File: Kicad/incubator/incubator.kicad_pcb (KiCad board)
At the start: 2 copper layers, 36 parts, among them J1 Barrel_Jack_MountingPin, J3 Conn_02x03_Odd_Even, J4 RJ12, J5 Conn_01x05, SW2 Rotary_Encoder_Switch, U1 AP63205WU, U2 ATmega328P-AU

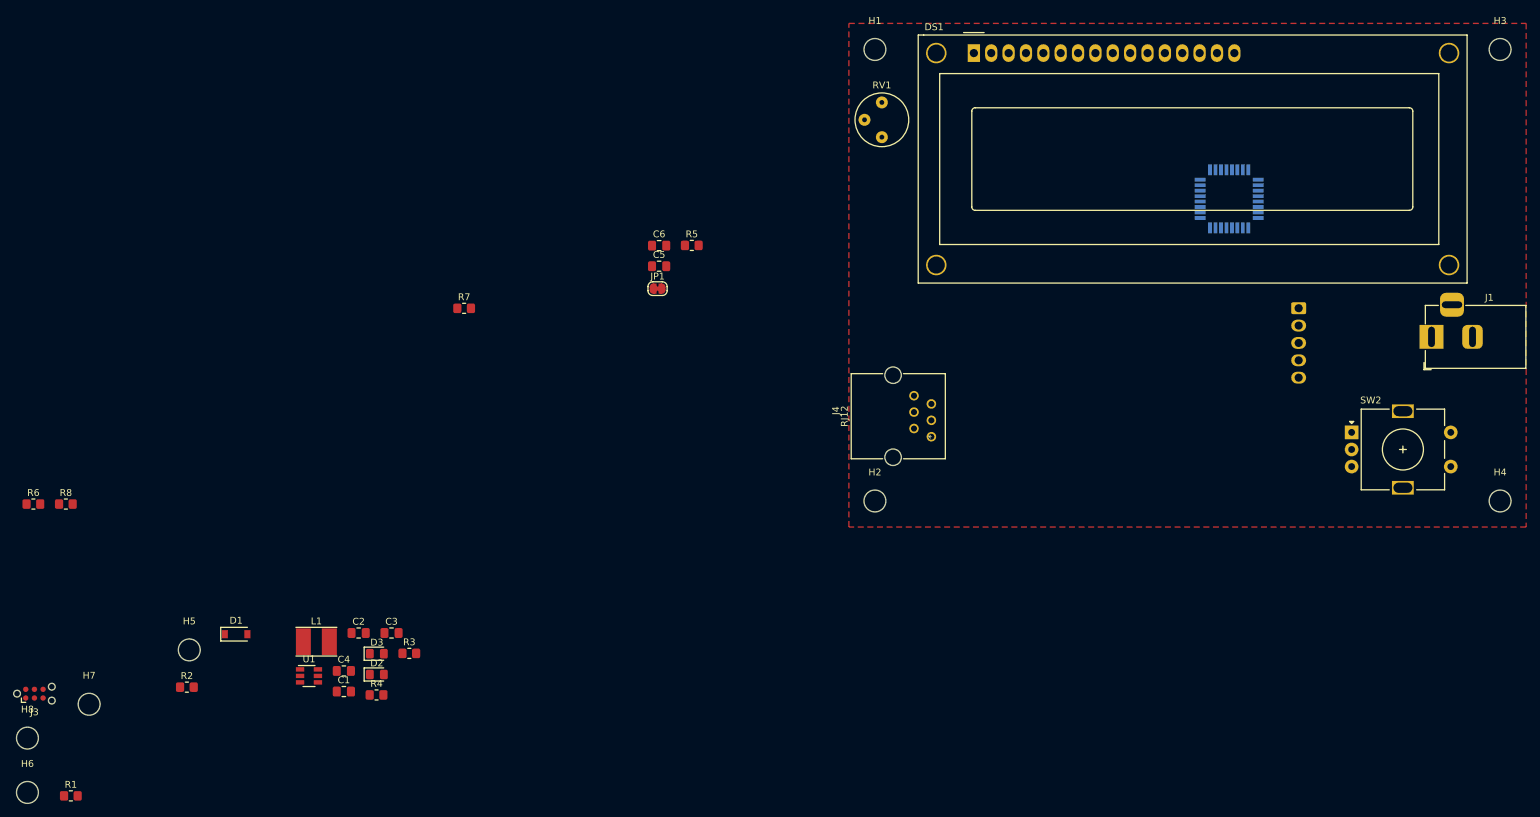
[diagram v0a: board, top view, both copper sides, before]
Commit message: fix: outline for incubator board
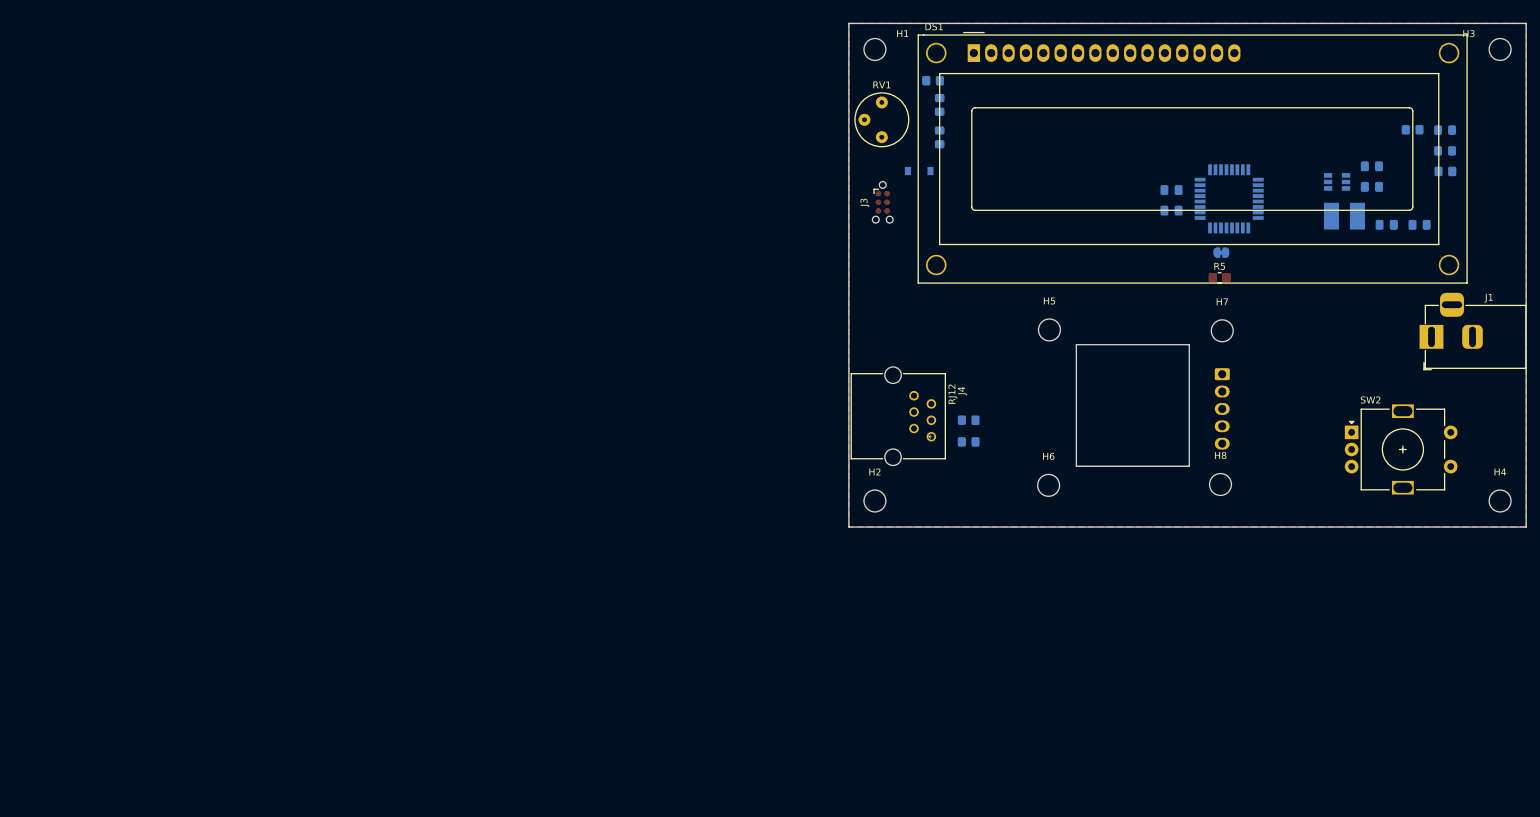
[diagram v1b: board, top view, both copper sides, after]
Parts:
- C1, C2, C3, C4, C5, C6, D1, D2, D3, JP1, L1, R1, R2, R3, R4, R6, R7, R8, U1: moved to B.Cu
- moved H8 178.4 mm to (79.5, 92.8)
- moved H7 174.5 mm to (79.8, 70.4)
- moved R4 174.1 mm to (112.4, 47.0), turned to 180 degrees
- moved D2 174.0 mm to (112.3, 44.0), turned to 180 degrees
- moved D3 174.0 mm to (112.3, 41.0), turned to 180 degrees
- moved C1 168.9 mm to (101.6, 46.3)
- moved U1 166.8 mm to (96.5, 48.6)
- moved C4 166.2 mm to (101.6, 49.3)
- moved R3 165.5 mm to (107.6, 41.0), turned to 180 degrees
- moved L1 162.7 mm to (97.6, 53.6)
- moved C2 161.8 mm to (103.8, 54.9)
- moved C3 161.8 mm to (108.6, 54.9)
- moved H6 156.0 mm to (54.4, 93.0)
- moved R6 144.8 mm to (38.4, 37.3), turned to 270 degrees
- moved J3 143.4 mm to (30.1, 51.6), turned to 270 degrees
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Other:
- board outline added: 99.1 x 73.7 mm
